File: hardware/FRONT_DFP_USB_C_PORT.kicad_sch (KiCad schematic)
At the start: 31 parts, among them J5 USB4200-03-A (VIRT FLAG MOUNT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, Q18 PMOS

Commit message: finaliseing pcb layout will come back later for a fresh look
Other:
- company: (none) -> MICK MAKE
- title: (none) -> 200W USB PD 3.1 HUB
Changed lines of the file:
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@@
 (kicad_sch (version 20230121) (generator eeschema)
   (paper "A4")
+  (title_block
+    (title "200W USB PD 3.1 HUB")
+    (date "2023-10-03")
+    (rev "A")
+    (company "MICK MAKE")
+    (comment 1 "THIS IS A 2X 100W USB PD SOURCE ")
+    (comment 2 "HUB USB SPEC 3.1")
+    (comment 3 "TOTAL SYSTEM POWER IS ~275w")
+  )
   (junction (at 128.27 186.69) (diameter 0) (color 0 0 0 0)
   )

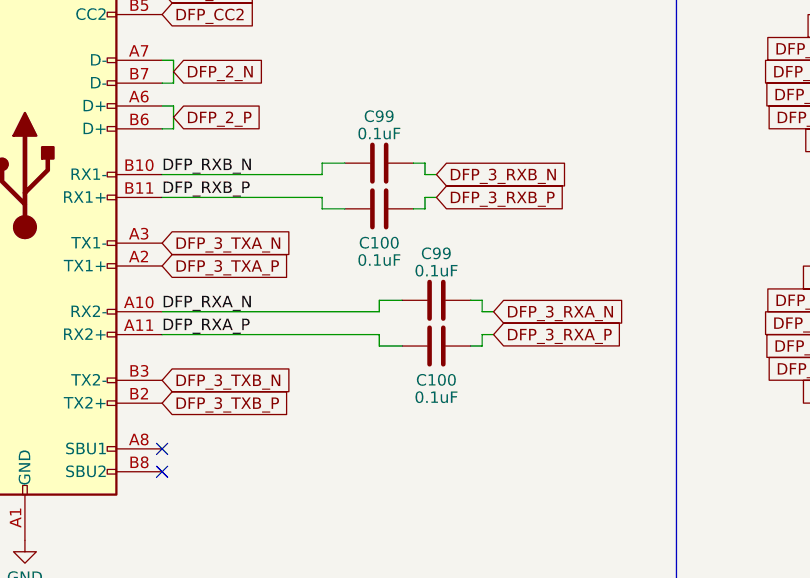
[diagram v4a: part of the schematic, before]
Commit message: working on fixing pcb impeedance
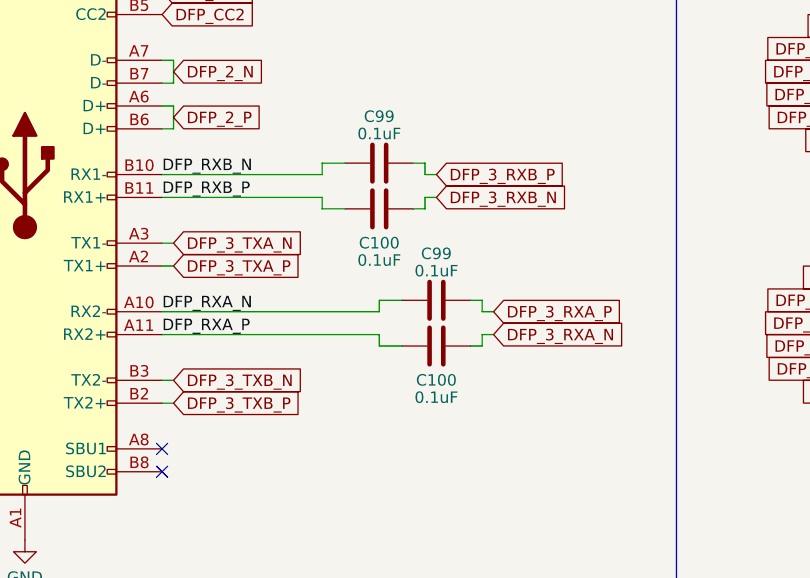
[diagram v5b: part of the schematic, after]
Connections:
- net DFP_3_RXA_N: now also C100.1; no longer C99.2
- net DFP_3_RXA_P: now also C99.2; no longer C100.1
- net DFP_3_RXB_N: now also C100.1; no longer C99.2
- net DFP_3_RXB_P: now also C99.2; no longer C100.1
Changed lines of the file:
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@@
+    (stroke (width 0) (type default))
+  )
+  (wire (pts (xy 55.88 77.47) (xy 57.15 77.47))
+    (stroke (width 0) (type default))
+  )
+  (wire (pts (xy 55.88 80.01) (xy 57.15 80.01))
     (stroke (width 0) (type default))
   )
@@
     (stroke (width 0) (type default))
   )
+  (wire (pts (xy 55.88 62.23) (xy 57.15 62.23))
+    (stroke (width 0) (type default))
+  )
   (wire (pts (xy 55.88 49.53) (xy 57.15 49.53))
     (stroke (width 0) (type default))
@@
     (stroke (width 0) (type default))
   )
+  (wire (pts (xy 55.88 64.77) (xy 57.15 64.77))
+    (stroke (width 0) (type default))
+  )
   (wire (pts (xy 162.56 157.48) (xy 168.91 157.48))
     (stroke (width 0) (type default))
@@
     (effects (font (size 1.27 1.27)) (justify left bottom))
   )
-  (global_label "DFP_3_TXB_P" (shape input) (at 55.88 80.01 0) (fields_autoplaced)
-    (effects (font (size 1.27 1.27)) (justify left))
-    (property "Intersheetrefs" "${INTERSHEET_REFS}" (at 71.2438 80.01 0)
+  (global_label "DFP_3_TXB_P" (shape input) (at 57.15 80.01 0) (fields_autoplaced)
+    (effects (font (size 1.27 1.27)) (justify left))
+    (property "Intersheetrefs" "${INTERSHEET_REFS}" (at 72.5138 80.01 0)
       (effects (font (size 1.27 1.27)) (justify left) hide)
     )
@@
     )
   )
-  (global_label "DFP_3_TXA_N" (shape input) (at 55.88 62.23 0) (fields_autoplaced)
-    (effects (font (size 1.27 1.27)) (justify left))
-    (property "Intersheetrefs" "${INTERSHEET_REFS}" (at 71.1229 62.23 0)
+  (global_label "DFP_3_TXA_N" (shape input) (at 57.15 62.23 0) (fields_autoplaced)
+    (effects (font (size 1.27 1.27)) (justify left))
+    (property "Intersheetrefs" "${INTERSHEET_REFS}" (at 72.3929 62.23 0)
       (effects (font (size 1.27 1.27)) (justify left) hide)
     )
@@
     )
   )
-  (global_label "DFP_3_TXB_N" (shape input) (at 55.88 77.47 0) (fields_autoplaced)
-    (effects (font (size 1.27 1.27)) (justify left))
-    (property "Intersheetrefs" "${INTERSHEET_REFS}" (at 71.3043 77.47 0)
+  (global_label "DFP_3_TXB_N" (shape input) (at 57.15 77.47 0) (fields_autoplaced)
+    (effects (font (size 1.27 1.27)) (justify left))
+    (property "Intersheetrefs" "${INTERSHEET_REFS}" (at 72.5743 77.47 0)
       (effects (font (size 1.27 1.27)) (justify left) hide)
     )
@@
     )
   )
-  (global_label "DFP_3_RXB_P" (shape input) (at 86.36 57.15 0) (fields_autoplaced)
-    (effects (font (size 1.27 1.27)) (justify left))
-    (property "Intersheetrefs" "${INTERSHEET_REFS}" (at 102.0262 57.15 0)
+  (global_label "DFP_3_RXB_P" (shape input) (at 86.36 54.61 0) (fields_autoplaced)
+    (effects (font (size 1.27 1.27)) (justify left))
+    (property "Intersheetrefs" "${INTERSHEET_REFS}" (at 102.0262 54.61 0)
       (effects (font (size 1.27 1.27)) (justify left) hide)
     )
@@
     )
   )
-  (global_label "DFP_3_RXB_N" (shape input) (at 86.36 54.61 0) (fields_autoplaced)
-    (effects (font (size 1.27 1.27)) (justify left))
-    (property "Intersheetrefs" "${INTERSHEET_REFS}" (at 102.0867 54.61 0)
+  (global_label "DFP_3_RXB_N" (shape input) (at 86.36 57.15 0) (fields_autoplaced)
+    (effects (font (size 1.27 1.27)) (justify left))
+    (property "Intersheetrefs" "${INTERSHEET_REFS}" (at 102.0867 57.15 0)
       (effects (font (size 1.27 1.27)) (justify left) hide)
     )
@@
     )
   )
-  (global_label "DFP_3_RXA_N" (shape input) (at 92.71 69.85 0) (fields_autoplaced)
-    (effects (font (size 1.27 1.27)) (justify left))
-    (property "Intersheetrefs" "${INTERSHEET_REFS}" (at 108.2553 69.85 0)
-      (effects (font (size 1.27 1.27)) (justify left) hide)
-    )
-  )
-  (global_label "DFP_3_TXA_P" (shape input) (at 55.88 64.77 0) (fields_autoplaced)
-    (effects (font (size 1.27 1.27)) (justify left))
-    (property "Intersheetrefs" "${INTERSHEET_REFS}" (at 71.0624 64.77 0)
+  (global_label "DFP_3_RXA_N" (shape input) (at 92.71 72.39 0) (fields_autoplaced)
+    (effects (font (size 1.27 1.27)) (justify left))
+    (property "Intersheetrefs" "${INTERSHEET_REFS}" (at 108.2553 72.39 0)
+      (effects (font (size 1.27 1.27)) (justify left) hide)
+    )
+  )
+  (global_label "DFP_3_TXA_P" (shape input) (at 57.15 64.77 0) (fields_autoplaced)
+    (effects (font (size 1.27 1.27)) (justify left))
+    (property "Intersheetrefs" "${INTERSHEET_REFS}" (at 72.3324 64.77 0)
       (effects (font (size 1.27 1.27)) (justify left) hide)
     )
@@
     )
   )
-  (global_label "DFP_3_RXA_P" (shape input) (at 92.71 72.39 0) (fields_autoplaced)
-    (effects (font (size 1.27 1.27)) (justify left))
-    (property "Intersheetrefs" "${INTERSHEET_REFS}" (at 108.1948 72.39 0)
-      (effects (font (size 1.27 1.27)) (justify left) hide)
-    )
+  (global_label "DFP_3_RXA_P" (shape input) (at 92.71 69.85 0) (fields_autoplaced)
+    (effects (font (size 1.27 1.27)) (justify left))
+    (property "Intersheetrefs" "${INTERSHEET_REFS}" (at 108.1948 69.85 0)
+      (effects (font (size 1.27 1.27)) (justify left) hide)
+    )

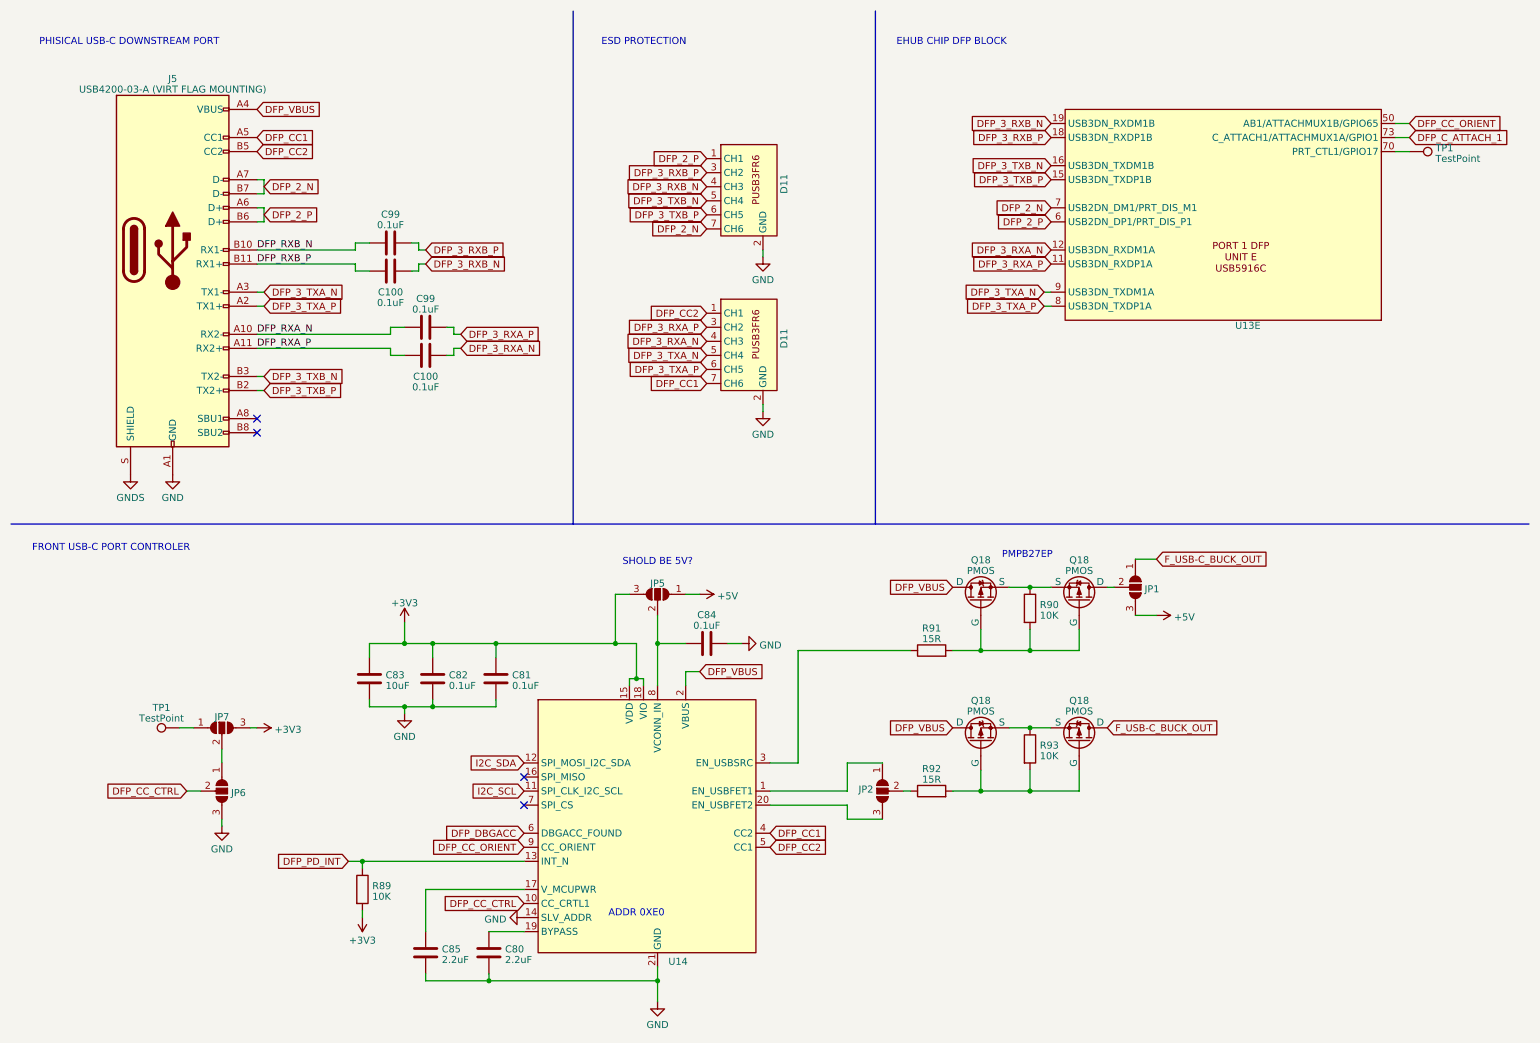
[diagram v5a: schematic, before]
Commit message: fixed DP issues and finneshed overall routeing
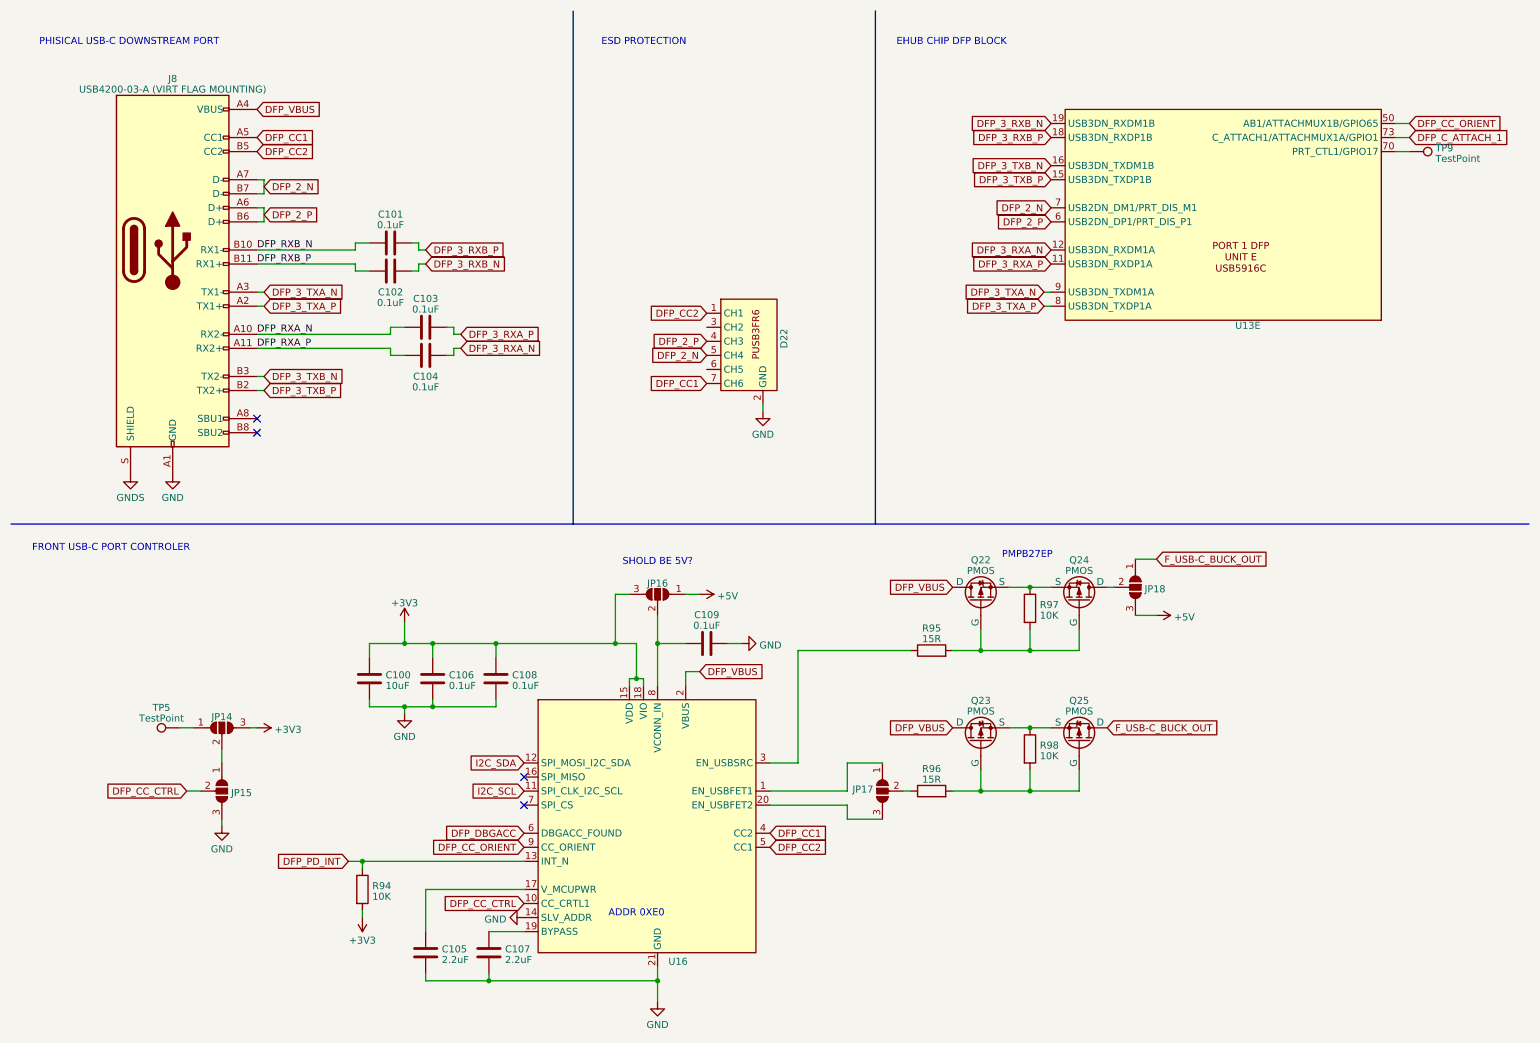
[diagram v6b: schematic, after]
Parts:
- removed D11: ~, CARTHING:PUSB3AB6Z_NEX, symbol CARTHING:PUSB3FR6
- renumbered C83 to C100, C99 to C101, C100 to C102, C99 to C103, C100 to C104, C85 to C105, C82 to C106, C80 to C107, C81 to C108, C84 to C109, D11 to D22, J5 to J8, JP7 to JP14, JP6 to JP15, JP5 to JP16, JP2 to JP17, JP1 to JP18, Q18 to Q22, Q18 to Q23, Q18 to Q24, Q18 to Q25, R89 to R94, R91 to R95, R92 to R96, R90 to R97, R93 to R98, TP1 to TP5, TP1 to TP9, U14 to U16
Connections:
- net DFP_2_N: now also D22.5 (CH4)
- net DFP_2_P: now also D22.4 (CH3)
- net DFP_3_RXA_N: no longer D22.4 (CH3)
- net DFP_3_RXA_P: no longer D22.3 (CH2)
- net DFP_3_TXA_N: no longer D22.5 (CH4)
- net DFP_3_TXA_P: no longer D22.6 (CH5)

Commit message: minor revisions
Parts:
- D22: value ~ -> PUSB3AB6Z
- Q22, Q23, Q24, Q25: value PMOS -> PMPB09R5VPX
- U13: value ~ -> USB5926C
- U16: value ~ -> PTN5100BMSP
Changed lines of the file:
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@@
       (effects (font (size 1.27 1.27)))
     )
-    (property "Value" "PMOS" (at 204.47 112.5761 90)
+    (property "Value" "PMPB09R5VPX" (at 204.47 112.5761 90)
       (effects (font (size 1.27 1.27)))
     )
@@
       (effects (font (size 1.27 1.27)))
     )
-    (property "Value" "PMOS" (at 186.69 112.5761 90)
+    (property "Value" "PMPB09R5VPX" (at 186.69 112.5761 90)
       (effects (font (size 1.27 1.27)))
     )
@@
       (effects (font (size 1.27 1.27)))
     )
-    (property "Value" "PMOS" (at 186.69 137.9761 90)
+    (property "Value" "PMPB09R5VPX" (at 186.69 137.9761 90)
       (effects (font (size 1.27 1.27)))
     )
@@
       (effects (font (size 1.27 1.27)))
     )
-    (property "Value" "PMOS" (at 204.47 137.9761 90)
+    (property "Value" "PMPB09R5VPX" (at 204.47 137.9761 90)
       (effects (font (size 1.27 1.27)))
     )
@@
   )
   (symbol (lib_id "CARTHING:USB5916C") (at 233.68 55.88 180) (unit 5)
-    (in_bom yes) (on_board yes) (dnp no) (fields_autoplaced)
+    (in_bom yes) (on_board yes) (dnp no)
     (property "Reference" "U13" (at 234.95 68.2719 0)
       (effects (font (size 1.27 1.27)))
     )
-    (property "Value" "~" (at 241.3 87.63 0)
+    (property "Value" "USB5926C" (at 254 27.94 0)
       (effects (font (size 1.27 1.27)))
     )
@@
       (effects (font (size 1.27 1.27)) (justify left))
     )
-    (property "Value" "~" (at 138.43 53.34 0)
+    (property "Value" "PUSB3AB6Z" (at 146.05 62.23 0)
       (effects (font (size 1.27 1.27)))
     )
@@
       (effects (font (size 1.27 1.27)) (justify left))
     )
-    (property "Value" "~" (at 102.87 127 0)
-      (effects (font (size 1.27 1.27)))
-    )
+    (property "Value" "PTN5100BMSP" (at 102.87 127 0)
+      (effects (font (size 1.27 1.27)))
+    )

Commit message: working on complie issues
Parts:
- added JP22: ~, Jumper:SolderJumper-2_P1.3mm_Open_RoundedPad1.0x1.5mm, symbol Jumper:SolderJumper_2_Open
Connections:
- net DFP_CC_ORIENT: now also JP22.2 (B); no longer U16.9 (CC_ORIENT)
- new net: JP22.1 (A), U16.9 (CC_ORIENT)
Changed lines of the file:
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@@
+    (stroke (width 0) (type default))
+  )
+  (wire (pts (xy 90.17 162.56) (xy 104.14 162.56))
     (stroke (width 0) (type default))
   )
@@
     )
   )
-  (global_label "DFP_CC_ORIENT" (shape input) (at 104.14 162.56 180) (fields_autoplaced)
-    (effects (font (size 1.27 1.27)) (justify right))
-    (property "Intersheetrefs" "${INTERSHEET_REFS}" (at 86.478 162.56 0)
+  (global_label "DFP_CC_ORIENT" (shape input) (at 82.55 162.56 180) (fields_autoplaced)
+    (effects (font (size 1.27 1.27)) (justify right))
+    (property "Intersheetrefs" "${INTERSHEET_REFS}" (at 64.888 162.56 0)
       (effects (font (size 1.27 1.27)) (justify right) hide)
     )
@@
         )
       )
+    )
+  )
+  (symbol (lib_id "Jumper:SolderJumper_2_Open") (at 86.36 162.56 180) (unit 1)
+    (in_bom yes) (on_board yes) (dnp no) (fields_autoplaced)
+    (property "Reference" "JP22" (at 86.36 160.5821 0)
+      (effects (font (size 1.27 1.27)))
+    )
+    (property "Value" "~" (at 87.6373 160.909 90)
+      (effects (font (size 1.27 1.27)) (justify right))
+    )
+    (property "Footprint" "Jumper:SolderJumper-2_P1.3mm_Open_RoundedPad1.0x1.5mm" (at 86.36 162.56 0)
+      (effects (font (size 1.27 1.27)) hide)
+    )
+    (property "Datasheet" "~" (at 86.36 162.56 0)
+      (effects (font (size 1.27 1.27)) hide)
+    )
+    (pin "1")
+    (pin "2")
+    (instances
+      (project "usbc-car-module"
+        (path "/fae025e9-99c5-40c1-af6f-99dc1edbfa43/ad0dde3f-c33d-40ce-8876-17a95cda421b"
+          (reference "JP22") (unit 1)
+        )
+      )
